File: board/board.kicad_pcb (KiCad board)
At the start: 2 copper layers, 45 x 13 mm, 17 parts, among them J1 002_SPI, J2 007_ADC, U1 MAX31855KASA

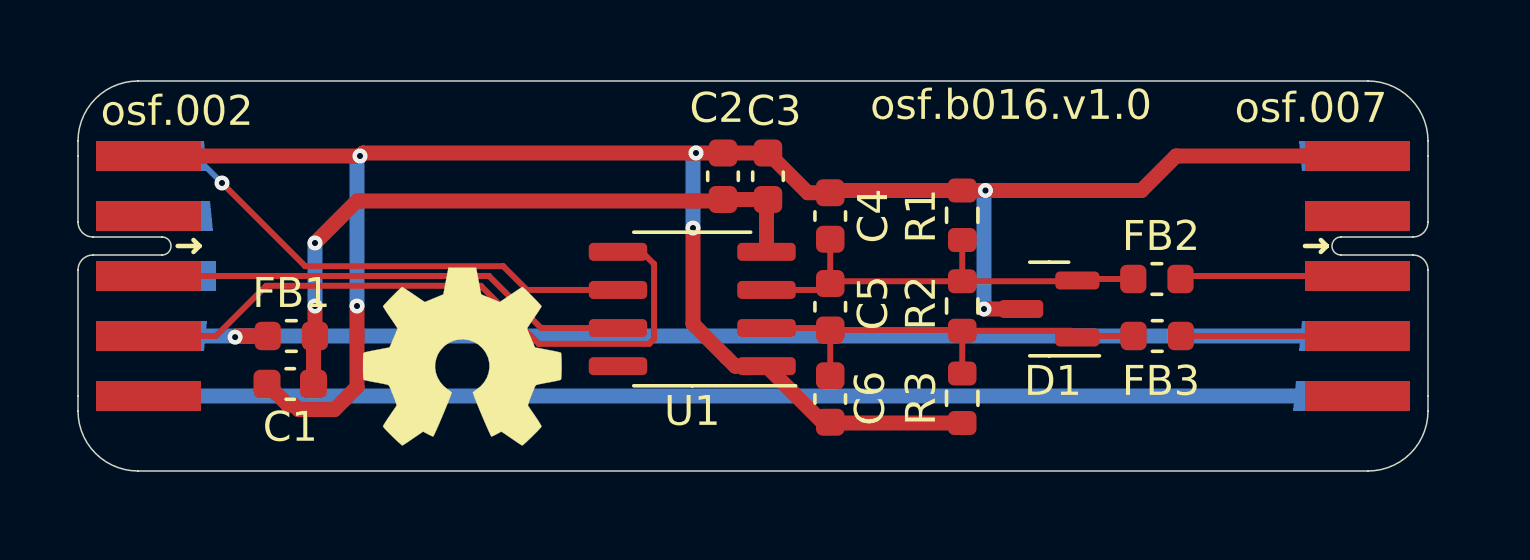
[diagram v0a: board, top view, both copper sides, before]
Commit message: added copper pours
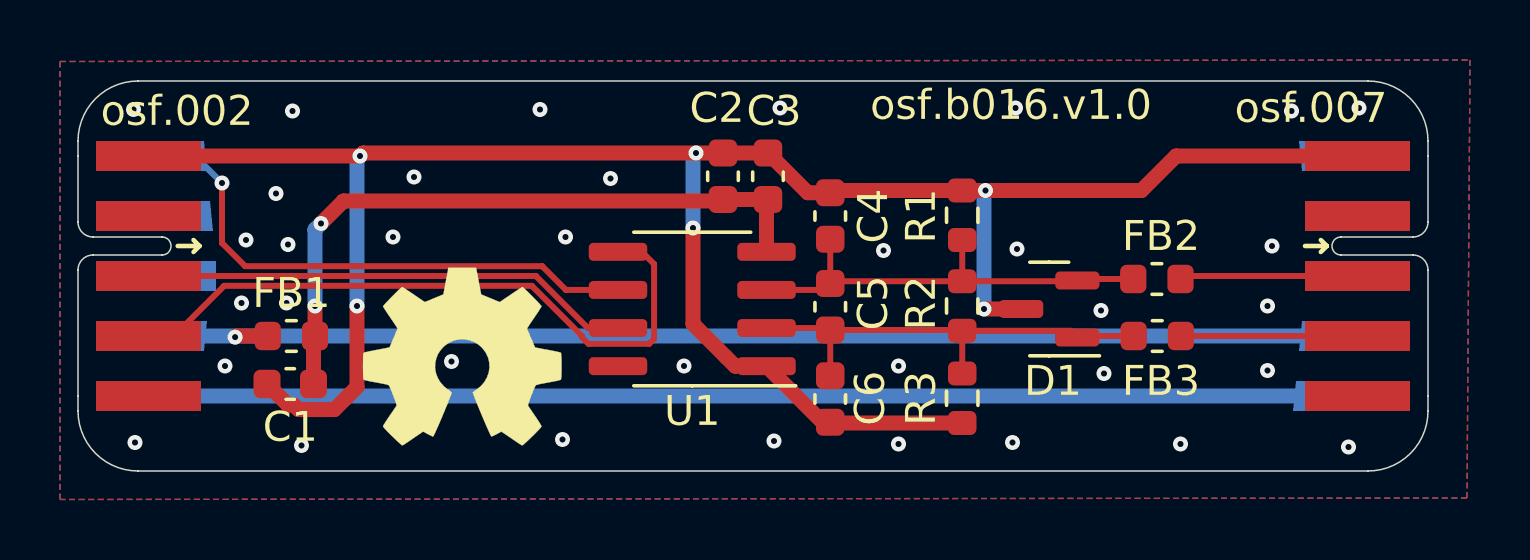
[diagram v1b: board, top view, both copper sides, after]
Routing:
- net /thermocouple/CS: track 17.4 -> 18.6 mm
- net GND: vias 6 -> 41
- added copper zone on B.Cu, net GND
- added copper zone on F.Cu, net GND
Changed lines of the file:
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@@
   (segment (start 147.85 100.1) (end 147.85 98.55) (width 0.5) (layer "F.Cu") (net 1))
   (segment (start 147.85 98.55) (end 147.9 98.5) (width 0.5) (layer "F.Cu") (net 1))
+  (segment (start 147.9 98.5) (end 147.9 97.5) (width 0.5) (layer "F.Cu") (net 1))
+  (segment (start 148.85 94) (end 161.45 94) (width 0.5) (layer "F.Cu") (net 1))
+  (segment (start 162.95 95.695) (end 162.95 94) (width 0.5) (layer "F.Cu") (net 1))
   (segment (start 161.45 94) (end 161.5 93.95) (width 0.5) (layer "F.Cu") (net 1))
-  (segment (start 147.9 95.4) (end 149.3 94) (width 0.5) (layer "F.Cu") (net 1))
-  (segment (start 147.9 98.5) (end 147.9 97.5) (width 0.5) (layer "F.Cu") (net 1))
-  (segment (start 162.95 95.695) (end 162.95 94) (width 0.5) (layer "F.Cu") (net 1))
   (segment (start 162.95 94) (end 163 93.95) (width 0.5) (layer "F.Cu") (net 1))
-  (segment (start 149.3 94) (end 161.45 94) (width 0.5) (layer "F.Cu") (net 1))
+  (segment (start 148.1 94.75) (end 148.85 94) (width 0.5) (layer "F.Cu") (net 1))
   (segment (start 161.5 93.95) (end 163 93.95) (width 0.5) (layer "F.Cu") (net 1))
   (via (at 147.9 97.5) (size 0.5) (drill 0.2) (layers "F.Cu" "B.Cu") (net 1))
-  (via (at 147.9 95.4) (size 0.5) (drill 0.2) (layers "F.Cu" "B.Cu") (net 1))
-  (segment (start 147.9 97.5) (end 147.9 95.4) (width 0.5) (layer "B.Cu") (net 1))
+  (via (at 148.1 94.75) (size 0.5) (drill 0.2) (layers "F.Cu" "B.Cu") (net 1))
+  (segment (start 147.9 94.95) (end 148.1 94.75) (width 0.5) (layer "B.Cu") (net 1))
+  (segment (start 147.9 97.5) (end 147.9 94.95) (width 0.5) (layer "B.Cu") (net 1))
   (segment (start 147 100.8) (end 147.2 100.8) (width 0.5) (layer "F.Cu") (net 2))
   (segment (start 163 92.4) (end 161.5 92.4) (width 0.5) (layer "F.Cu") (net 2))
@@
   (segment (start 147.352 100.952) (end 148.548 100.952) (width 0.5) (layer "F.Cu") (net 2))
   (segment (start 147.2 100.8) (end 147.352 100.952) (width 0.5) (layer "F.Cu") (net 2))
+  (via (at 147.45 102.15) (size 0.5) (drill 0.2) (layers "F.Cu" "B.Cu") (free) (net 2))
+  (via (at 179.65 97.5) (size 0.5) (drill 0.2) (layers "F.Cu" "B.Cu") (free) (net 2))
+  (via (at 179.8 95.5) (size 0.5) (drill 0.2) (layers "F.Cu" "B.Cu") (free) (net 2))
+  (via (at 152.45 99.35) (size 0.5) (drill 0.2) (layers "F.Cu" "B.Cu") (free) (net 2))
   (via (at 149.3 97.5) (size 0.5) (drill 0.2) (layers "F.Cu" "B.Cu") (net 2))
+  (via (at 156.15 101.95) (size 0.5) (drill 0.2) (layers "F.Cu" "B.Cu") (free) (net 2))
+  (via (at 151.2 93.2) (size 0.5) (drill 0.2) (layers "F.Cu" "B.Cu") (free) (net 2))
+  (via (at 174.2 99.75) (size 0.5) (drill 0.2) (layers "F.Cu" "B.Cu") (free) (net 2))
+  (via (at 156.25 95.2) (size 0.5) (drill 0.2) (layers "F.Cu" "B.Cu") (free) (net 2))
+  (via (at 182.35 102.2) (size 0.5) (drill 0.2) (layers "F.Cu" "B.Cu") (free) (net 2))
+  (via (at 167.35 102.1) (size 0.5) (drill 0.2) (layers "F.Cu" "B.Cu") (free) (net 2))
+  (via (at 171.25 90.9) (size 0.5) (drill 0.2) (layers "F.Cu" "B.Cu") (free) (net 2))
+  (via (at 166.85 95.65) (size 0.5) (drill 0.2) (layers "F.Cu" "B.Cu") (free) (net 2))
+  (via (at 160.2 99.5) (size 0.5) (drill 0.2) (layers "F.Cu" "B.Cu") (free) (net 2))
+  (via (at 145.6 95.3) (size 0.5) (drill 0.2) (layers "F.Cu" "B.Cu") (free) (net 2))
+  (via (at 146.95 97.4) (size 0.5) (drill 0.2) (layers "F.Cu" "B.Cu") (free) (net 2))
+  (via (at 176.75 102.1) (size 0.5) (drill 0.2) (layers "F.Cu" "B.Cu") (free) (net 2))
+  (via (at 146.6 93.75) (size 0.5) (drill 0.2) (layers "F.Cu" "B.Cu") (free) (net 2))
+  (via (at 145.45 97.4) (size 0.5) (drill 0.2) (layers "F.Cu" "B.Cu") (free) (net 2))
+  (via (at 174.1 97.65) (size 0.5) (drill 0.2) (layers "F.Cu" "B.Cu") (free) (net 2))
+  (via (at 167.35 99.5) (size 0.5) (drill 0.2) (layers "F.Cu" "B.Cu") (free) (net 2))
+  (via (at 179.65 99.65) (size 0.5) (drill 0.2) (layers "F.Cu" "B.Cu") (free) (net 2))
+  (via (at 171.3 95.6) (size 0.5) (drill 0.2) (layers "F.Cu" "B.Cu") (free) (net 2))
   (via (at 170.25 93.65) (size 0.5) (drill 0.2) (layers "F.Cu" "B.Cu") (net 2))
+  (via (at 150.5 95.2) (size 0.5) (drill 0.2) (layers "F.Cu" "B.Cu") (free) (net 2))
   (via (at 160.6 92.4) (size 0.5) (drill 0.2) (layers "F.Cu" "B.Cu") (net 2))
   (via (at 170.2 97.6) (size 0.5) (drill 0.2) (layers "F.Cu" "B.Cu") (net 2))
+  (via (at 147.15 91) (size 0.5) (drill 0.2) (layers "F.Cu" "B.Cu") (free) (net 2))
+  (via (at 182.7 90.9) (size 0.5) (drill 0.2) (layers "F.Cu" "B.Cu") (free) (net 2))
+  (via (at 171.15 102.05) (size 0.5) (drill 0.2) (layers "F.Cu" "B.Cu") (free) (net 2))
   (via (at 160.5 94.9) (size 0.5) (drill 0.2) (layers "F.Cu" "B.Cu") (net 2))
+  (via (at 147 95.45) (size 0.5) (drill 0.2) (layers "F.Cu" "B.Cu") (free) (net 2))
+  (via (at 163.4 90.9) (size 0.5) (drill 0.2) (layers "F.Cu" "B.Cu") (free) (net 2))
+  (via (at 180.45 91) (size 0.5) (drill 0.2) (layers "F.Cu" "B.Cu") (free) (net 2))
+  (via (at 141.9 102.05) (size 0.5) (drill 0.2) (layers "F.Cu" "B.Cu") (free) (net 2))
+  (via (at 163.2 102) (size 0.5) (drill 0.2) (layers "F.Cu" "B.Cu") (free) (net 2))
+  (via (at 141.85 90.95) (size 0.5) (drill 0.2) (layers "F.Cu" "B.Cu") (free) (net 2))
+  (via (at 155.4 90.95) (size 0.5) (drill 0.2) (layers "F.Cu" "B.Cu") (free) (net 2))
   (via (at 149.4 92.5) (size 0.5) (drill 0.2) (layers "F.Cu" "B.Cu") (net 2))
+  (via (at 144.9 99.5) (size 0.5) (drill 0.2) (layers "F.Cu" "B.Cu") (free) (net 2))
+  (via (at 157.75 93.25) (size 0.5) (drill 0.2) (layers "F.Cu" "B.Cu") (free) (net 2))
   (segment (start 160.5 92.5) (end 160.6 92.4) (width 0.5) (layer "B.Cu") (net 2))
   (segment (start 160.5 94.9) (end 160.5 92.5) (width 0.5) (layer "B.Cu") (net 2))
@@
   (segment (start 176.85 96.5) (end 182.65 96.5) (width 0.2) (layer "F.Cu") (net 5))
   (segment (start 176.7625 98.5) (end 182.65 98.5) (width 0.2) (layer "F.Cu") (net 6))
-  (segment (start 155.362 98.762) (end 159.038 98.762) (width 0.2) (layer "F.Cu") (net 7))
+  (segment (start 157.018841 98.762) (end 159.038 98.762) (width 0.2) (layer "F.Cu") (net 7))
+  (segment (start 156.798 98.498) (end 156.798 98.541159) (width 0.2) (layer "F.Cu") (net 7))
+  (segment (start 159.202 98.598) (end 159.202 96.102) (width 0.2) (layer "F.Cu") (net 7))
+  (segment (start 158.795 95.695) (end 158 95.695) (width 0.2) (layer "F.Cu") (net 7))
+  (segment (start 156.798 98.541159) (end 157.018841 98.762) (width 0.2) (layer "F.Cu") (net 7))
+  (segment (start 159.202 96.102) (end 158.795 95.695) (width 0.2) (layer "F.Cu") (net 7))
   (segment (start 159.038 98.762) (end 159.202 98.598) (width 0.2) (layer "F.Cu") (net 7))
-  (segment (start 146.273 96.827) (end 153.427 96.827) (width 0.2) (layer "F.Cu") (net 7))
-  (segment (start 159.202 98.598) (end 159.202 96.102) (width 0.2) (layer "F.Cu") (net 7))
-  (segment (start 159.202 96.102) (end 158.795 95.695) (width 0.2) (layer "F.Cu") (net 7))
-  (segment (start 153.427 96.827) (end 155.362 98.762) (width 0.2) (layer "F.Cu") (net 7))
-  (segment (start 158.795 95.695) (end 158 95.695) (width 0.2) (layer "F.Cu") (net 7))
-  (segment (start 144.6 98.5) (end 146.273 96.827) (width 0.2) (layer "F.Cu") (net 7))
-  (segment (start 142.35 98.5) (end 144.6 98.5) (width 0.2) (layer "F.Cu") (net 7))
-  (segment (start 154.965 96.965) (end 154.173 96.173) (width 0.2) (layer "F.Cu") (net 8))
-  (segment (start 147.573 96.173) (end 144.8 93.4) (width 0.2) (layer "F.Cu") (net 8))
-  (segment (start 158 96.965) (end 154.965 96.965) (width 0.2) (layer "F.Cu") (net 8))
-  (segment (start 154.173 96.173) (end 147.573 96.173) (width 0.2) (layer "F.Cu") (net 8))
+  (segment (start 144.873 96.827) (end 155.127 96.827) (width 0.2) (layer "F.Cu") (net 7))
+  (segment (start 142.35 98.5) (end 143.2 98.5) (width 0.2) (layer "F.Cu") (net 7))
+  (segment (start 155.127 96.827) (end 156.798 98.498) (width 0.2) (layer "F.Cu") (net 7))
+  (segment (start 143.2 98.5) (end 144.873 96.827) (width 0.2) (layer "F.Cu") (net 7))
+  (segment (start 144.8 95.4) (end 144.8 93.4) (width 0.2) (layer "F.Cu") (net 8))
+  (segment (start 155.473 96.173) (end 145.573 96.173) (width 0.2) (layer "F.Cu") (net 8))
+  (segment (start 158 96.965) (end 156.265 96.965) (width 0.2) (layer "F.Cu") (net 8))
+  (segment (start 145.573 96.173) (end 144.8 95.4) (width 0.2) (layer "F.Cu") (net 8))
+  (segment (start 156.265 96.965) (end 155.473 96.173) (width 0.2) (layer "F.Cu") (net 8))
   (via (at 144.8 93.4) (size 0.5) (drill 0.2) (layers "F.Cu" "B.Cu") (net 8))
   (segment (start 143.9 92.5) (end 142.4 92.5) (width 0.2) (layer "B.Cu") (net 8))
   (segment (start 144.8 93.4) (end 143.9 92.5) (width 0.2) (layer "B.Cu") (net 8))
-  (segment (start 155.435 98.235) (end 153.7 96.5) (width 0.2) (layer "F.Cu") (net 9))
-  (segment (start 153.7 96.5) (end 142.35 96.5) (width 0.2) (layer "F.Cu") (net 9))
-  (segment (start 158 98.235) (end 155.435 98.235) (width 0.2) (layer "F.Cu") (net 9))
+  (segment (start 155.262448 96.5) (end 142.35 96.5) (width 0.2) (layer "F.Cu") (net 9))
+  (segment (start 156.997448 98.235) (end 155.262448 96.5) (width 0.2) (layer "F.Cu") (net 9))
+  (segment (start 158 98.235) (end 156.997448 98.235) (width 0.2) (layer "F.Cu") (net 9))
   (segment (start 145.27458 98.5) (end 145.23729 98.53729) (width 0.5) (layer "F.Cu") (net 10))
   (segment (start 146.325 98.5) (end 145.27458 98.5) (width 0.5) (layer "F.Cu") (net 10))
@@
   (segment (start 142.4 98.5) (end 182.6 98.5) (width 0.5) (layer "B.Cu") (net 10))
   (segment (start 142.3 100.5) (end 182.5 100.5) (width 0.5) (layer "B.Cu") (net 15))
+  (zone (net 2) (net_name "GND") (layers F&B.Cu) (hatch edge 0.508)
+    (connect_pads (clearance 0.2))
+    (min_thickness 0.2) (filled_areas_thickness no)
+    (fill yes (thermal_gap 0.508) (thermal_bridge_width 0.508))
+    (polygon
+      (pts
+        (xy 186.3 103.9)
+        (xy 139.4 103.95)
+        (xy 139.4 89.35)
+        (xy 186.4 89.3)
+      )
+    )
+  )
 )
